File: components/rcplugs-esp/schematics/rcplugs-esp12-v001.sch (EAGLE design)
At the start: 12 parts, among them IC1 MCP1700TT3302

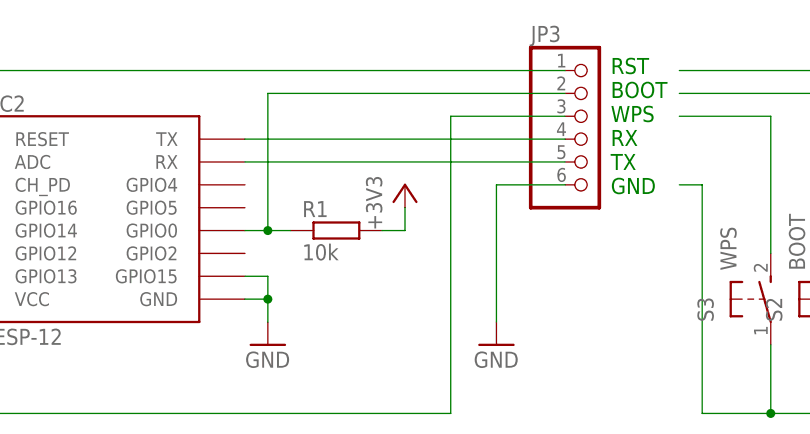
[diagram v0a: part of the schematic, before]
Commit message: v27: added output of some status information (.Info) to mqtt, fixed schematics issue with rx/tx
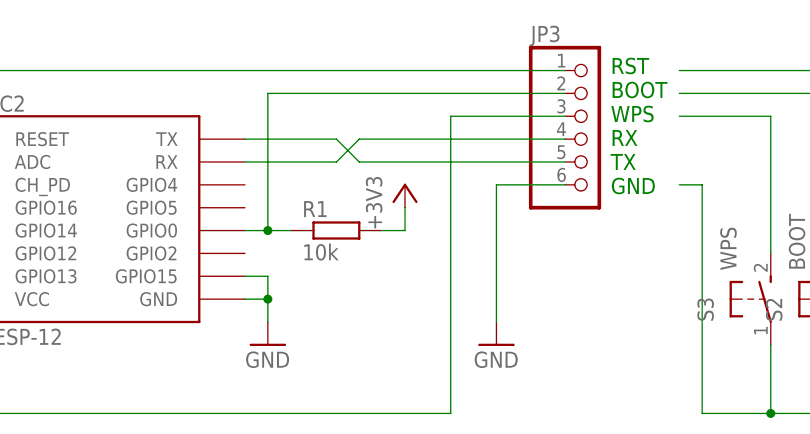
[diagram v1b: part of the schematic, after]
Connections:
- net N$2: now also JP3.5; no longer JP3.4
- net N$3: now also JP3.4; no longer JP3.5
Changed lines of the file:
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@@
 <setting verticaltext="up"/>
 </settings>
-<grid distance="0.1" unitdist="inch" unit="inch" style="lines" multiple="1" display="yes" altdistance="0.01" altunitdist="inch" altunit="inch"/>
+<grid distance="0.1" unitdist="inch" unit="inch" style="lines" multiple="1" display="no" altdistance="0.01" altunitdist="inch" altunit="inch"/>
 <layers>
 <layer number="1" name="Top" color="4" fill="1" visible="no" active="no"/>
@@
 </segment>
 </net>
-<net name="N$2" class="0">
-<segment>
-<wire x1="38.1" y1="121.92" x2="73.66" y2="121.92" width="0.1524" layer="91"/>
-<pinref part="IC2" gate="G$1" pin="TX"/>
-<pinref part="JP3" gate="A" pin="4"/>
-</segment>
-</net>
-<net name="N$3" class="0">
-<segment>
-<wire x1="38.1" y1="119.38" x2="73.66" y2="119.38" width="0.1524" layer="91"/>
-<pinref part="IC2" gate="G$1" pin="RX"/>
-<pinref part="JP3" gate="A" pin="5"/>
-</segment>
-</net>
 <net name="N$4" class="0">
 <segment>
@@
 </segment>
 </net>
+<net name="N$2" class="0">
+<segment>
+<pinref part="IC2" gate="G$1" pin="TX"/>
+<wire x1="38.1" y1="121.92" x2="48.26" y2="121.92" width="0.1524" layer="91"/>
+<wire x1="48.26" y1="121.92" x2="50.8" y2="119.38" width="0.1524" layer="91"/>
+<pinref part="JP3" gate="A" pin="5"/>
+<wire x1="50.8" y1="119.38" x2="73.66" y2="119.38" width="0.1524" layer="91"/>
+</segment>
+</net>
+<net name="N$3" class="0">
+<segment>
+<pinref part="IC2" gate="G$1" pin="RX"/>
+<wire x1="38.1" y1="119.38" x2="48.26" y2="119.38" width="0.1524" layer="91"/>
+<wire x1="48.26" y1="119.38" x2="50.8" y2="121.92" width="0.1524" layer="91"/>
+<pinref part="JP3" gate="A" pin="4"/>
+<wire x1="50.8" y1="121.92" x2="73.66" y2="121.92" width="0.1524" layer="91"/>
+</segment>
+</net>
